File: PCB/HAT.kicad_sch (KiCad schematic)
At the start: 0 parts

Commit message: MERGING SCHEMATICS
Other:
- added sheet MicroController_Interfacing (microcontroller_interfacing.kicad_sch)
- sheet Power Module ports: added 3V3, GND, USB_IN_5V, V_BAT+; removed none
- sheet Sensor Module ports: added +V_BAT, 3V3, A0, GND, GPIO_STM, SCL_STM, SDA_STM; removed none
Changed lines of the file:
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@@
 (kicad_sch (version 20230121) (generator eeschema)
   (paper "A4")
+  (junction (at 127 38.1) (diameter 0) (color 0 0 0 0)
+  )
+  (wire (pts (xy 113.03 38.1) (xy 127 38.1))
+    (stroke (width 0) (type default))
+  )
+  (wire (pts (xy 127 38.1) (xy 127 76.2))
+    (stroke (width 0) (type default))
+  )
+  (wire (pts (xy 153.67 60.96) (xy 156.21 60.96))
+    (stroke (width 0) (type default))
+  )
+  (wire (pts (xy 77.47 76.2) (xy 77.47 92.71))
+    (stroke (width 0) (type default))
+  )
+  (wire (pts (xy 154.94 66.04) (xy 156.21 66.04))
+    (stroke (width 0) (type default))
+  )
+  (wire (pts (xy 101.6 92.71) (xy 101.6 81.28))
+    (stroke (width 0) (type default))
+  )
+  (wire (pts (xy 127 38.1) (xy 156.21 38.1))
+    (stroke (width 0) (type default))
+  )
+  (wire (pts (xy 114.3 109.22) (xy 154.94 109.22))
+    (stroke (width 0) (type default))
+  )
+  (wire (pts (xy 154.94 109.22) (xy 154.94 66.04))
+    (stroke (width 0) (type default))
+  )
+  (wire (pts (xy 114.3 96.52) (xy 144.78 96.52))
+    (stroke (width 0) (type default))
+  )
+  (wire (pts (xy 116.84 57.15) (xy 113.03 57.15))
+    (stroke (width 0) (type default))
+  )
+  (wire (pts (xy 113.03 43.18) (xy 156.21 43.18))
+    (stroke (width 0) (type default))
+  )
+  (wire (pts (xy 114.3 105.41) (xy 153.67 105.41))
+    (stroke (width 0) (type default))
+  )
+  (wire (pts (xy 149.86 55.88) (xy 156.21 55.88))
+    (stroke (width 0) (type default))
+  )
+  (wire (pts (xy 101.6 81.28) (xy 116.84 81.28))
+    (stroke (width 0) (type default))
+  )
+  (wire (pts (xy 114.3 100.33) (xy 149.86 100.33))
+    (stroke (width 0) (type default))
+  )
+  (wire (pts (xy 127 76.2) (xy 77.47 76.2))
+    (stroke (width 0) (type default))
+  )
+  (wire (pts (xy 156.21 52.07) (xy 144.78 52.07))
+    (stroke (width 0) (type default))
+  )
+  (wire (pts (xy 153.67 105.41) (xy 153.67 60.96))
+    (stroke (width 0) (type default))
+  )
+  (wire (pts (xy 116.84 81.28) (xy 116.84 57.15))
+    (stroke (width 0) (type default))
+  )
+  (wire (pts (xy 149.86 100.33) (xy 149.86 55.88))
+    (stroke (width 0) (type default))
+  )
+  (wire (pts (xy 113.03 46.99) (xy 156.21 46.99))
+    (stroke (width 0) (type default))
+  )
+  (wire (pts (xy 144.78 52.07) (xy 144.78 96.52))
+    (stroke (width 0) (type default))
+  )
   (sheet (at 40.64 30.48) (size 72.39 36.83) (fields_autoplaced)
     (stroke (width 0.1524) (type solid))
@@
     (property "Sheetfile" "Power_Module.kicad_sch" (at 40.64 67.8946 0)
       (effects (font (size 1.27 1.27)) (justify left top))
+    )
+    (pin "3V3" output (at 113.03 38.1 0)
+      (effects (font (size 1.27 1.27)) (justify right))
+    )
+    (pin "V_BAT+" output (at 113.03 43.18 0)
+      (effects (font (size 1.27 1.27)) (justify right))
+    )
+    (pin "USB_IN_5V" input (at 113.03 57.15 0)
+      (effects (font (size 1.27 1.27)) (justify right))
+    )
+    (pin "GND" bidirectional (at 113.03 46.99 0)
+      (effects (font (size 1.27 1.27)) (justify right))
     )
     (instances
@@
       (effects (font (size 1.27 1.27)) (justify left top))
     )
+    (pin "3V3" input (at 156.21 38.1 180)
+      (effects (font (size 1.27 1.27)) (justify left))
+    )
+    (pin "SDA_STM" input (at 156.21 66.04 180)
+      (effects (font (size 1.27 1.27)) (justify left))
+    )
+    (pin "SCL_STM" input (at 156.21 60.96 180)
+      (effects (font (size 1.27 1.27)) (justify left))
+    )
+    (pin "GPIO_STM" input (at 156.21 55.88 180)
+      (effects (font (size 1.27 1.27)) (justify left))
+    )
+    (pin "A0" input (at 156.21 52.07 180)
+      (effects (font (size 1.27 1.27)) (justify left))
+    )
+    (pin "+V_BAT" input (at 156.21 43.18 180)
+      (effects (font (size 1.27 1.27)) (justify left))
+    )
+    (pin "GND" bidirectional (at 156.21 46.99 180)
+      (effects (font (size 1.27 1.27)) (justify left))
+    )
     (instances
       (project "HAT"
@@
       )
     )
+  )
+  (sheet (at 41.91 92.71) (size 72.39 33.02) (fields_autoplaced)
+    (stroke (width 0.1524) (type solid))
+    (fill (color 0 0 0 0.0000))
+    (property "Sheetname" "MicroController_Interfacing" (at 41.91 91.9984 0)
+      (effects (font (size 1.27 1.27)) (justify left bottom))
+    )
+    (property "Sheetfile" "microcontroller_interfacing.kicad_sch" (at 41.91 126.3146 0)
+      (effects (font (size 1.27 1.27)) (justify left top))
+    )
+    (pin "DigitalSensorSCL" input (at 114.3 105.41 0)
+      (effects (font (size 1.27 1.27)) (justify right))
+    )
+    (pin "DigitalSensorSDA" input (at 114.3 109.22 0)
+      (effects (font (size 1.27 1.27)) (justify right))
+    )
+    (pin "GPIO 0" input (at 114.3 100.33 0)
+      (effects (font (size 1.27 1.27)) (justify right))
+    )
+    (pin "GPIO 1" input (at 114.3 114.3 0)
+      (effects (font (size 1.27 1.27)) (justify right))
+    )
+    (pin "USB 5V" input (at 101.6 92.71 90)
+      (effects (font (size 1.27 1.27)) (justify right))
+    )
+    (pin "A0" input (at 114.3 96.52 0)
+      (effects (font (size 1.27 1.27)) (justify right))
+    )
+    (pin "3V3" input (at 77.47 92.71 90)
+      (effects (font (size 1.27 1.27)) (justify right))
+    )
+    (instances
+      (project "HAT"
+        (path "/40f36b19-a08c-43e7-88a6-ec8387939712" (page "4"))
+      )
+    )

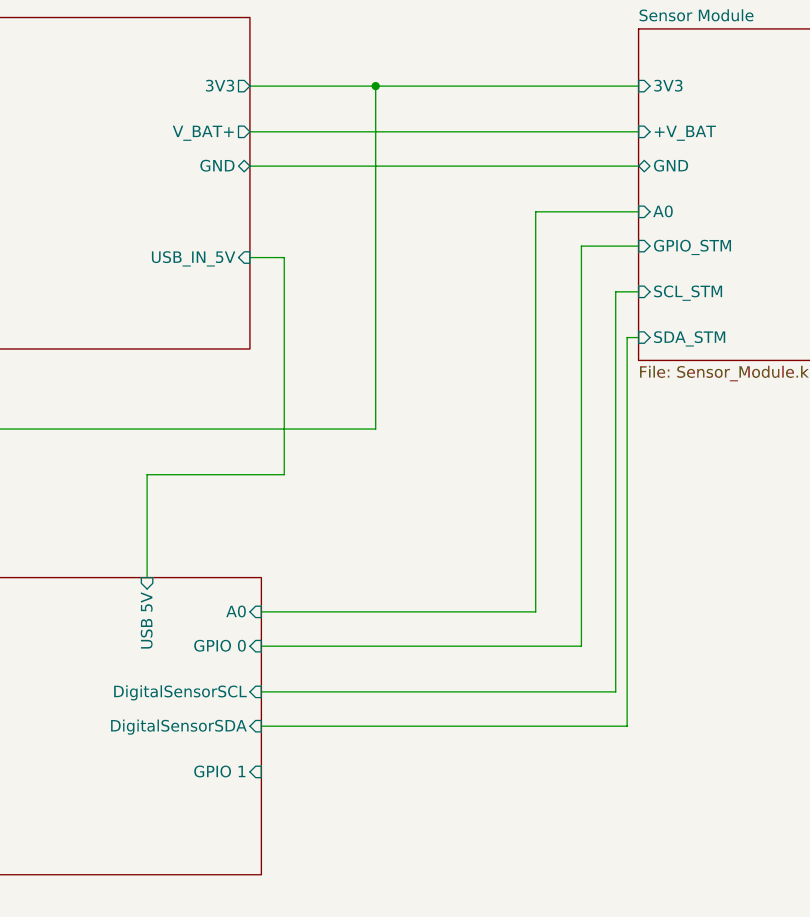
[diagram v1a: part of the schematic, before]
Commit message: Update MC Interfacing schematic
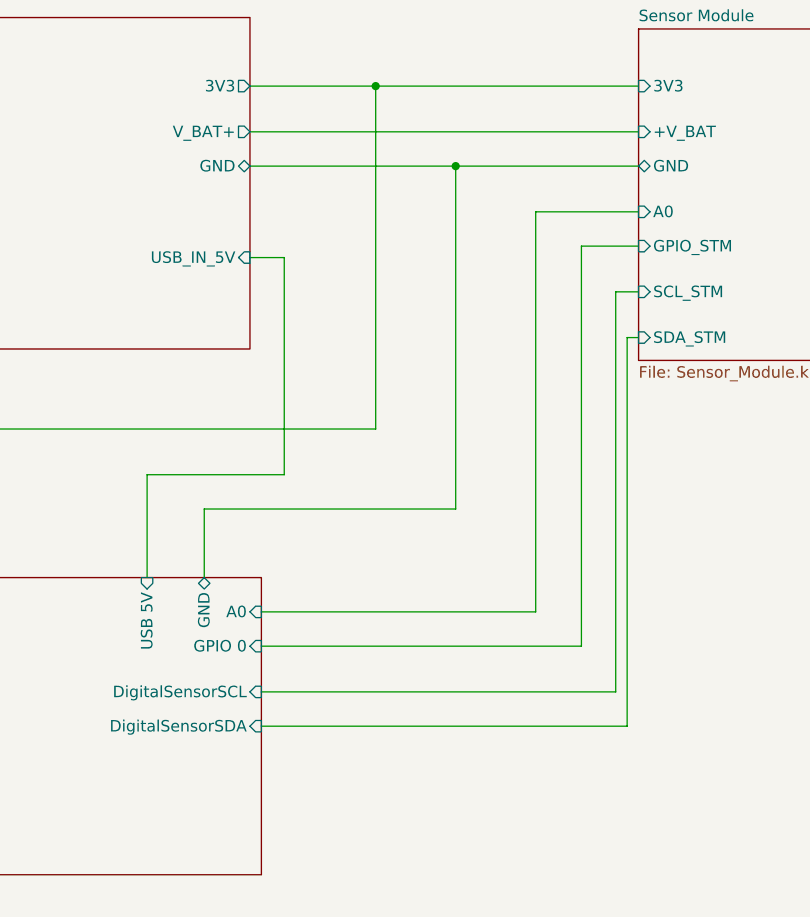
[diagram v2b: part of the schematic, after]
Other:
- sheet MicroController_Interfacing ports: added GND; removed GPIO 1
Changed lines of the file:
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@@
 (kicad_sch (version 20230121) (generator eeschema)
   (paper "A4")
+  (junction (at 135.89 46.99) (diameter 0) (color 0 0 0 0)
+  )
   (junction (at 127 38.1) (diameter 0) (color 0 0 0 0)
   )
@@
   )
   (wire (pts (xy 127 38.1) (xy 156.21 38.1))
+    (stroke (width 0) (type default))
+  )
+  (wire (pts (xy 135.89 46.99) (xy 156.21 46.99))
+    (stroke (width 0) (type default))
+  )
+  (wire (pts (xy 135.89 85.09) (xy 135.89 46.99))
     (stroke (width 0) (type default))
   )
@@
     (stroke (width 0) (type default))
   )
+  (wire (pts (xy 107.95 85.09) (xy 135.89 85.09))
+    (stroke (width 0) (type default))
+  )
   (wire (pts (xy 156.21 52.07) (xy 144.78 52.07))
+    (stroke (width 0) (type default))
+  )
+  (wire (pts (xy 107.95 92.71) (xy 107.95 85.09))
     (stroke (width 0) (type default))
   )
@@
     (stroke (width 0) (type default))
   )
-  (wire (pts (xy 113.03 46.99) (xy 156.21 46.99))
+  (wire (pts (xy 113.03 46.99) (xy 135.89 46.99))
     (stroke (width 0) (type default))
   )
@@
       (effects (font (size 1.27 1.27)) (justify right))
     )
-    (pin "GPIO 1" input (at 114.3 114.3 0)
-      (effects (font (size 1.27 1.27)) (justify right))
-    )
     (pin "USB 5V" input (at 101.6 92.71 90)
       (effects (font (size 1.27 1.27)) (justify right))
@@
       (effects (font (size 1.27 1.27)) (justify right))
     )
+    (pin "GND" bidirectional (at 107.95 92.71 90)
+      (effects (font (size 1.27 1.27)) (justify right))
+    )
